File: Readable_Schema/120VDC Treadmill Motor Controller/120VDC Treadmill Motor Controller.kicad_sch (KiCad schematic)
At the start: 0 parts

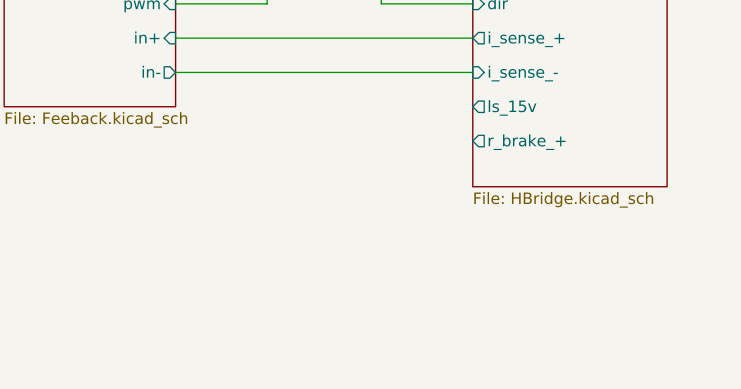
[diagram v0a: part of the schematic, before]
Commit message: Finished adding e stop circuit and roughly choosing a cap for high voltage line -- mostly to deal with ripple current. Almost done implementing the brake resistor subcircuit
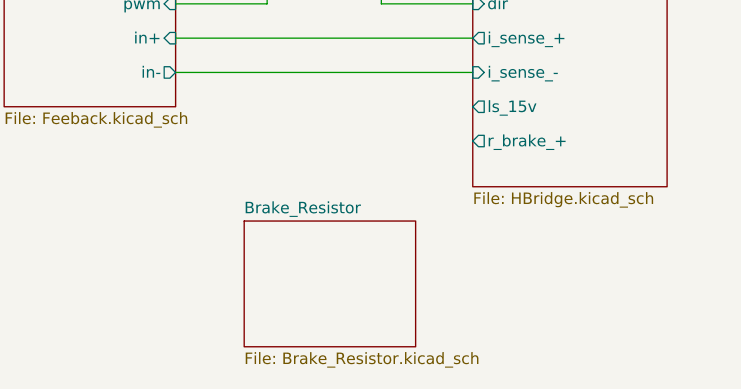
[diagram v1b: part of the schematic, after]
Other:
- added sheet Brake_Resistor (Brake_Resistor.kicad_sch)
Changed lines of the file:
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@@
+	)
+	(sheet
+		(at 130.81 128.27)
+		(size 19.05 13.97)
+		(exclude_from_sim no)
+		(in_bom yes)
+		(on_board yes)
+		(dnp no)
+		(fields_autoplaced yes)
+		(stroke
+			(width 0.1524)
+			(type solid)
+		)
+		(fill
+			(color 0 0 0 0.0000)
+		)
+		(property "Sheetname" "Brake_Resistor"
+			(at 130.81 127.5584 0)
+			(effects
+				(font
+					(size 1.27 1.27)
+				)
+				(justify left bottom)
+			)
+		)
+		(property "Sheetfile" "Brake_Resistor.kicad_sch"
+			(at 130.81 142.8246 0)
+			(effects
+				(font
+					(size 1.27 1.27)
+				)
+				(justify left top)
+			)
+		)
+		(instances
+			(project "120VDC Treadmill Motor Controller"
+				(path "/319bc5c0-2dd5-4df3-a34b-9170833ebccd"
+					(page "10")
+				)
+			)
+		)
 	)
 	(sheet

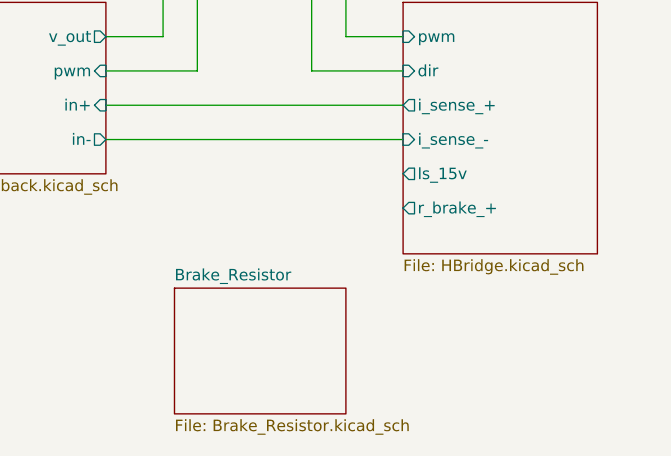
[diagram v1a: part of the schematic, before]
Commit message: we have reached the point of starting to roughly place where components should go (have not started messing with traces). -Confirm heatsink size so that we can block that area out on the schema -add some test points similar to what we were testing in ltspice to determine functionality of the device -Review general layout with dad to confirm we r good to start drawing traces
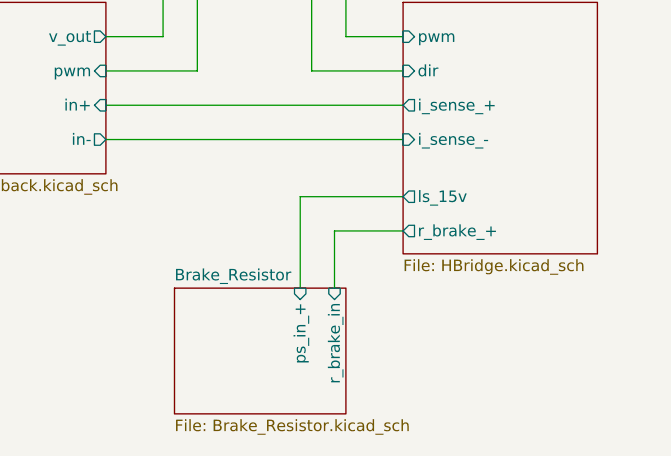
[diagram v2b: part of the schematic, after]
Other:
- sheet Brake_Resistor ports: added ps_in_+, r_brake_in; removed none
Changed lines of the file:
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@@
+	(wire
+		(pts
+			(xy 144.78 128.27) (xy 144.78 118.11)
+		)
+		(stroke
+			(width 0)
+			(type default)
+		)
+	)
 	(wire
 		(pts
@@
 	(wire
 		(pts
+			(xy 148.59 121.92) (xy 156.21 121.92)
+		)
+		(stroke
+			(width 0)
+			(type default)
+		)
+	)
+	(wire
+		(pts
 			(xy 149.86 88.9) (xy 149.86 83.82)
 		)
@@
 	(wire
 		(pts
+			(xy 144.78 118.11) (xy 156.21 118.11)
+		)
+		(stroke
+			(width 0)
+			(type default)
+		)
+	)
+	(wire
+		(pts
 			(xy 129.54 83.82) (xy 129.54 100.33)
+		)
+		(stroke
+			(width 0)
+			(type default)
+		)
+	)
+	(wire
+		(pts
+			(xy 148.59 128.27) (xy 148.59 121.92)
 		)
 		(stroke
@@
 		)
 		(pin "ls_15v" output
-			(at 156.21 115.57 180)
+			(at 156.21 118.11 180)
 			(effects
 				(font
@@
 		)
 		(pin "r_brake_+" output
-			(at 156.21 119.38 180)
+			(at 156.21 121.92 180)
 			(effects
 				(font
@@
 			)
 		)
+		(pin "r_brake_in" input
+			(at 148.59 128.27 90)
+			(effects
+				(font
+					(size 1.27 1.27)
+				)
+				(justify right)
+			)
+		)
+		(pin "ps_in_+" input
+			(at 144.78 128.27 90)
+			(effects
+				(font
+					(size 1.27 1.27)
+				)
+				(justify right)
+			)
+		)
